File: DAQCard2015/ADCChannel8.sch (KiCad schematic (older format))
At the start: 21 parts, among them U10 THS4524IDBTR, U11 AD9219

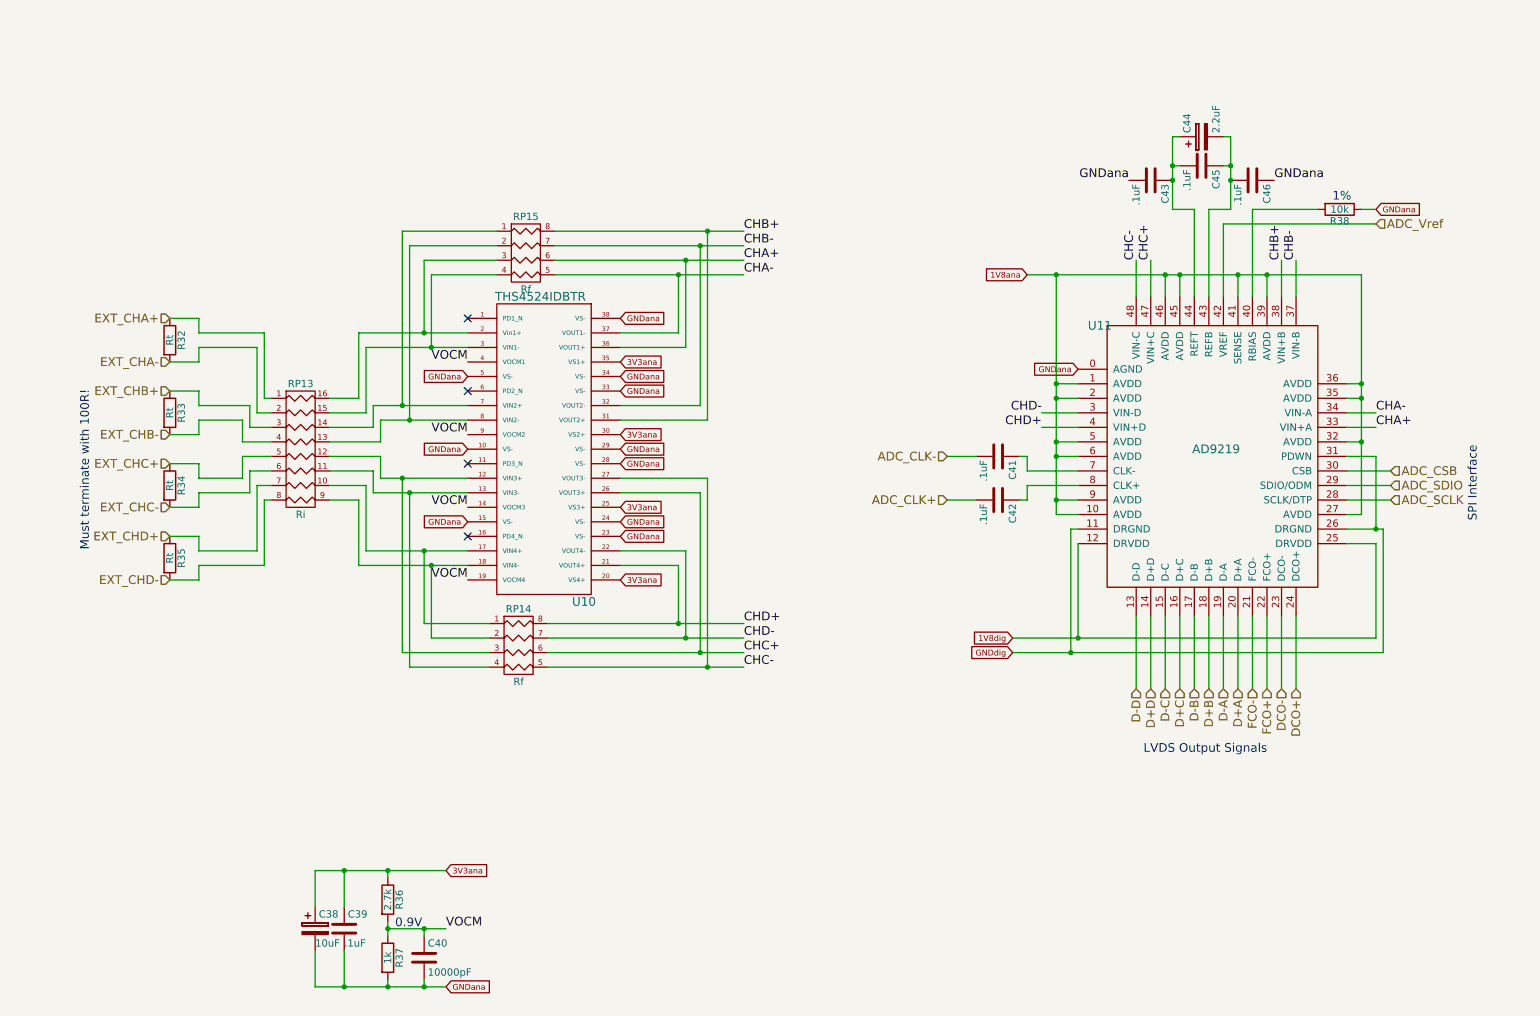
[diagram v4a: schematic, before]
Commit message: propogate previous changes to other channels and schematic
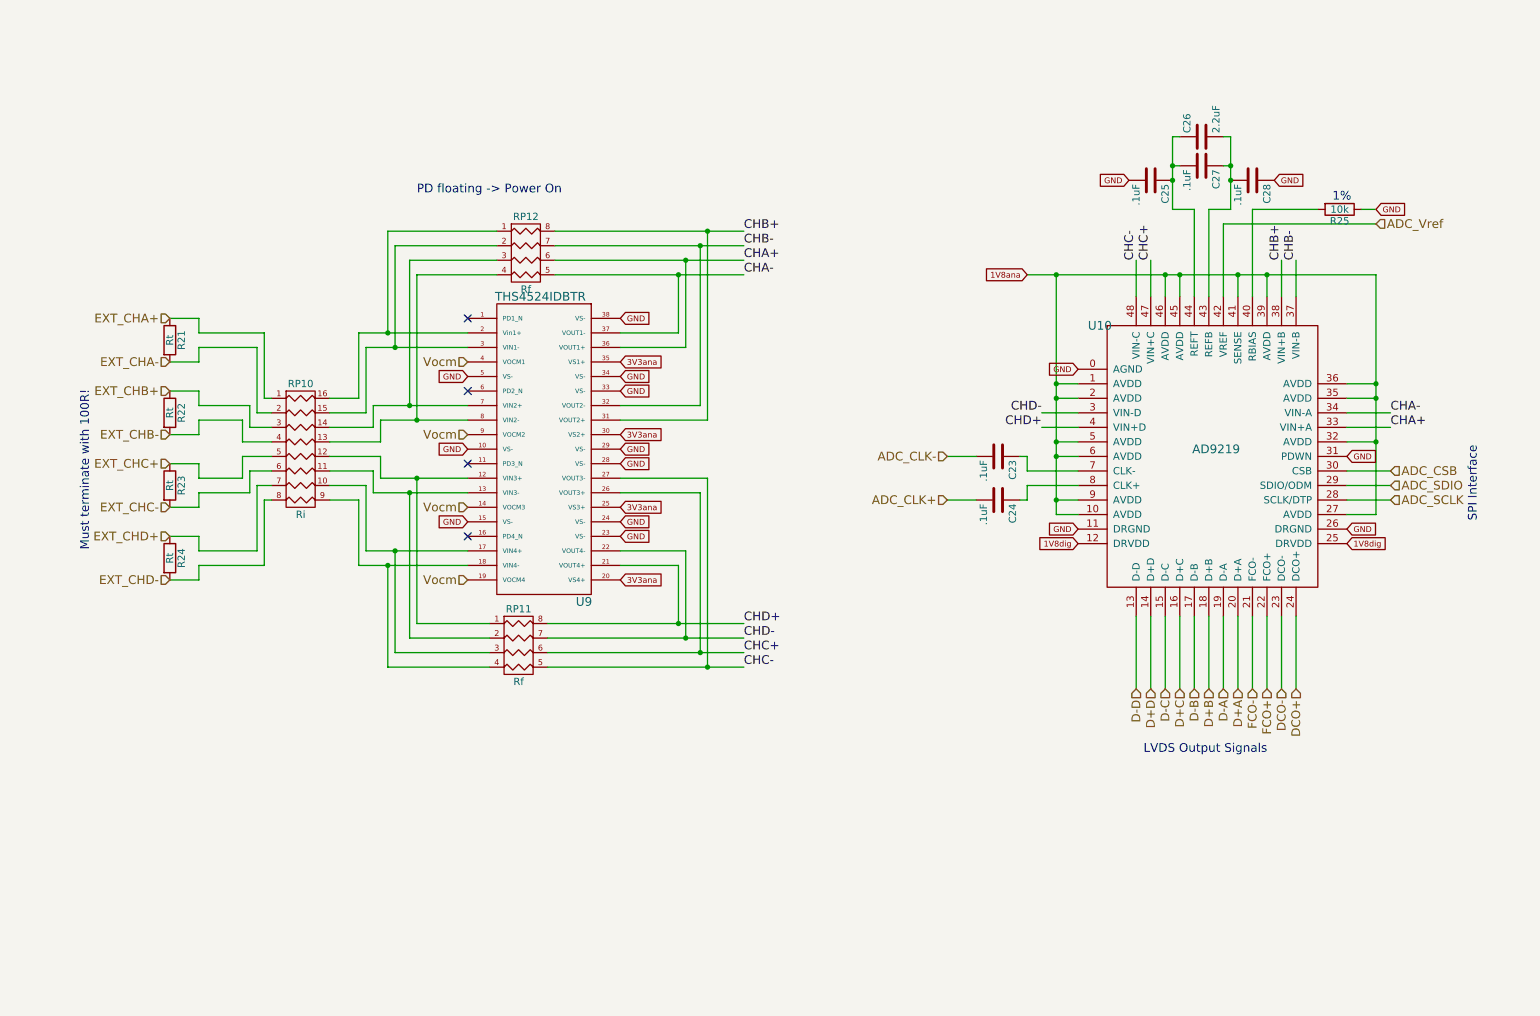
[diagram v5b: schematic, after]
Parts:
- removed C38: 10uF, Capacitors_SMD:C_0805, symbol CP
- removed C39, C41, C42, C43, C45, C46: .1uF, Capacitors_SMD:C_0603, symbol C
- removed C40: 10000pF, Capacitors_SMD:C_0603, symbol C
- removed C44: 2.2uF, Capacitors_SMD:C_0805, symbol CP
- removed R32, R33, R34, R35: Rt, Resistors_SMD:R_0603, symbol R
- removed R36: 2.7k, Resistors_SMD:R_0603, symbol R
- removed R37: 1k, Resistors_SMD:R_0603, symbol R
- removed R38: 10k, Resistors_SMD:R_0603, symbol R
- removed RP13: Ri, extras:R8_MNR18, symbol R_PACK8
- removed RP14, RP15: Rf, extras:R4-MNR04, symbol R_PACK4
- removed U10: THS4524IDBTR, Housings_SSOP:TSSOP-38_4.4x9.7mm_Pitch0.5mm, symbol THS4524IDBTR
- removed U11: AD9219, SMD_Packages:QFN-48-1EP, symbol AD9219
- added C23, C24, C25, C27, C28: .1uF, Capacitors_SMD:C_0603, symbol C
- added C26: 2.2uF, Capacitors_SMD:C_0805, symbol C
- added R21, R22, R23, R24: Rt, Resistors_SMD:R_0603, symbol R
- added R25: 10k, Resistors_SMD:R_0603, symbol R
- added RP10: Ri, extras:R8_MNR18, symbol R_PACK8
- added RP11, RP12: Rf, extras:R4-MNR04, symbol R_PACK4
- added U10: AD9219, extras:QFN-48-1EP, symbol AD9219
- added U9: THS4524IDBTR, Housings_SSOP:TSSOP-38_4.4x9.7mm_Pitch0.5mm, symbol THS4524IDBTR
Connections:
- net 1V8ana: now also U10.1 (AVDD), U10.10 (AVDD), U10.2 (AVDD), U10.27 (AVDD), U10.32 (AVDD), U10.35 (AVDD), U10.36 (AVDD), U10.39 (AVDD), U10.41 (SENSE), U10.45 (AVDD), U10.46 (AVDD), U10.5 (AVDD), U10.6 (AVDD), U10.9 (AVDD)
- net 1V8dig: now also U10.12 (DRVDD), U10.25 (DRVDD)
- net 3V3ana: now also U9.20 (VS4+), U9.25 (VS3+), U9.30 (VS2+), U9.35 (VS1+)
- net ADC_CLK+: now also C24.2
- net ADC_CLK-: now also C23.2
- net ADC_CSB: now also U10.30 (CSB)
- net ADC_SCLK: now also U10.28 (SCLK/DTP)
- net ADC_SDIO: now also U10.29 (SDIO/ODM)
- net ADC_Vref: now also U10.42 (VREF)
- net CHA+: now also RP12.6 (R3), U10.33 (VIN+A), U9.36 (VOUT1+)
- net CHA-: now also RP12.5 (R4), U10.34 (VIN-A), U9.37 (VOUT1-)
- net CHB+: now also RP12.8 (R1), U10.38 (VIN+B), U9.31 (VOUT2+)
- net CHB-: now also RP12.7 (R2), U10.37 (VIN-B), U9.32 (VOUT2-)
- net CHC+: now also RP11.6 (R3), U10.47 (VIN+C), U9.26 (VOUT3+)
- net CHC-: now also RP11.5 (R4), U10.48 (VIN-C), U9.27 (VOUT3-)
- net CHD+: now also RP11.8 (R1), U10.4 (VIN+D), U9.21 (VOUT4+)
- net CHD-: now also RP11.7 (R2), U10.3 (VIN-D), U9.22 (VOUT4-)
- net D+A: now also U10.20 (D+A)
- net D+B: now also U10.18 (D+B)
- net D+C: now also U10.16 (D+C)
- net D+D: now also U10.14 (D+D)
- net D-A: now also U10.19 (D-A)
- net D-B: now also U10.17 (D-B)
- net D-C: now also U10.15 (D-C)
- net D-D: now also U10.13 (D-D)
- net DCO+: now also U10.24 (DCO+)
- net DCO-: now also U10.23 (DCO-)
- net EXT_CHA+: now also R21.1, RP10.1 (P1)
- net EXT_CHA-: now also R21.2, RP10.2 (P2)
- net EXT_CHB+: now also R22.1, RP10.3 (P3)
- net EXT_CHB-: now also R22.2, RP10.4 (P4)
- net EXT_CHC+: now also R23.1, RP10.5 (P5)
- net EXT_CHC-: now also R23.2, RP10.6 (P6)
- net EXT_CHD+: now also R24.1, RP10.7 (P7)
- net EXT_CHD-: now also R24.2, RP10.8 (P8)
- net FCO+: now also U10.22 (FCO+)
- net FCO-: now also U10.21 (FCO-)
- new net: C24.1, U10.8 (CLK+)
- new net: RP10.16 (R1), RP12.1 (P1), U9.2 (Vin1+)
- new net: RP10.15 (R2), RP12.2 (P2), U9.3 (VIN1-)
- new net: RP10.14 (R3), RP12.3 (P3), U9.7 (VIN2+)
- new net: RP10.13 (R4), RP12.4 (P4), U9.8 (VIN2-)
- new net: R25.2, U10.40 (RBIAS)
- new net: C26.2, C27.1, C28.2, U10.43 (REFB)
- new net: C25.1, C26.1, C27.2, U10.44 (REFT)
- new net: C23.1, U10.7 (CLK-)
- new net: RP10.12 (R5), RP11.1 (P1), U9.12 (VIN3+)
- new net: RP10.11 (R6), RP11.2 (P2), U9.13 (VIN3-)
- new net: RP10.10 (R7), RP11.3 (P3), U9.17 (VIN4+)
- new net: RP10.9 (R8), RP11.4 (P4), U9.18 (VIN4-)
- new net GND: C25.2, C28.1, R25.1, U10.0 (AGND), U10.11 (DRGND), U10.26 (DRGND), U10.31 (PDWN), U9.10 (VS-), U9.15 (VS-), U9.23 (VS-), U9.24 (VS-), U9.28 (VS-), U9.29 (VS-), U9.33 (VS-), U9.34 (VS-), U9.38 (VS-), U9.5 (VS-)
- new net Vocm: U9.14 (VOCM3), U9.19 (VOCM4), U9.4 (VOCM1), U9.9 (VOCM2)
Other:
- note added: "PD floating -> Power On"
- note removed: "0.9V"

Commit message: Various updates to DAQ board focusing on power system
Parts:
- U9: footprint Housings_SSOP:TSSOP-38_4.4x9.7mm_Pitch0.5mm -> extras:TSSOP-38_4.4x9.7mm_Pitch0.5mm
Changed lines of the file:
@@
 F 0 "U9" H 4700 2750 60  0000 C CNN
 F 1 "THS4524IDBTR" H 4400 4850 60  0000 C CNN
-F 2 "Housings_SSOP:TSSOP-38_4.4x9.7mm_Pitch0.5mm" H 4600 3800 60  0001 C CNN
+F 2 "extras:TSSOP-38_4.4x9.7mm_Pitch0.5mm" H 4600 3800 60  0001 C CNN
 F 3 "" H 4600 3800 60  0000 C CNN
 	1    4400 3700

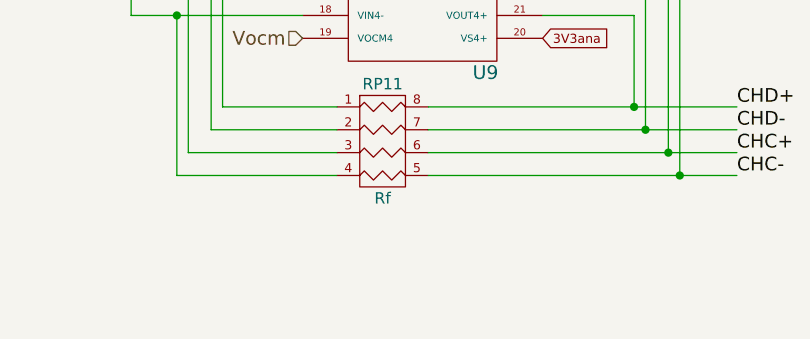
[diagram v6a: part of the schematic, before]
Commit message: Update to DAQ Board including adding an JTAG header and hooking up external clock and trigger
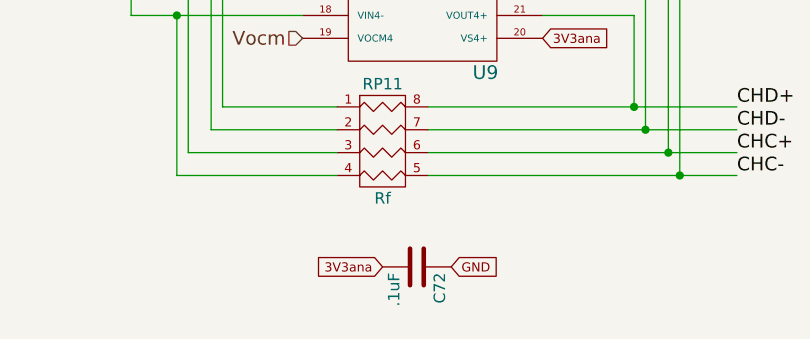
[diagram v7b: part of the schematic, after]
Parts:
- added C72: .1uF, Capacitors_SMD:C_0603, symbol C
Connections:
- net 3V3ana: now also C72.2
- net GND: now also C72.1
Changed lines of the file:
@@
 $Descr A4 11693 8268
 encoding utf-8
-Sheet 3 13
+Sheet 13 13
 Title ""
 Date ""
@@
 Text GLabel 8100 4150 0    40   Input ~ 0
 GND
+$Comp
+L C C72
+U 1 1 5605C69F
+P 4400 5500
+F 0 "C72" H 4425 5600 50  0000 L CNN
+F 1 ".1uF" H 4425 5400 50  0000 L CNN
+F 2 "Capacitors_SMD:C_0603" H 4438 5350 30  0001 C CNN
+F 3 "" H 4400 5500 60  0000 C CNN
+	1    4400 5500
+	0    1    1    0
+$EndComp
+Text GLabel 4250 5500 0    40   Input ~ 0
+3V3ana
+Text GLabel 4550 5500 2    40   Input ~ 0
+GND
 $EndSCHEMATC

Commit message: Adds digipart field to all parts that is now used in automatic generation of BOM(see DAQCard2015.html)
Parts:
- C23, C24, C25, C27, C28, C72: digipart (none) -> 445-1316-1-ND
- C26: digipart (none) -> 445-1420-1-ND
- R21, R22, R23, R24: digipart (none) -> P107HCT-ND
- R25: digipart (none) -> P10.0KHCT-ND
- RP10: digipart (none) -> RHM1564CT-ND
- RP11, RP12: digipart (none) -> RHM1336CT-ND
- U10: digipart (none) -> AD9219ABCPZ-40-ND
- U9: digipart (none) -> 296-24315-1-ND
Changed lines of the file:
@@
 F 2 "extras:QFN-48-1EP" H 8650 3700 60  0001 C CNN
 F 3 "" H 8650 3700 60  0000 C CNN
+F 4 "AD9219ABCPZ-40-ND" H 9050 3700 60  0001 C CNN "digipart"
 	1    9050 3700
 	1    0    0    -1
@@
 F 2 "Capacitors_SMD:C_0603" H 7588 3500 30  0001 C CNN
 F 3 "" H 7550 3650 60  0000 C CNN
+F 4 "445-1316-1-ND" H 7550 3650 60  0001 C CNN "digipart"
 	1    7550 3650
 	0    1    1    0
@@
 F 2 "Capacitors_SMD:C_0603" H 7588 3800 30  0001 C CNN
 F 3 "" H 7550 3950 60  0000 C CNN
+F 4 "445-1316-1-ND" H 7550 3950 60  0001 C CNN "digipart"
 	1    7550 3950
 	0    1    1    0
@@
 F 2 "Capacitors_SMD:C_0603" H 9338 1600 30  0001 C CNN
 F 3 "" H 9300 1750 60  0000 C CNN
+F 4 "445-1316-1-ND" H 9300 1750 60  0001 C CNN "digipart"
 	1    9300 1750
 	0    1    1    0
@@
 F 2 "Capacitors_SMD:C_0603" H 8638 1600 30  0001 C CNN
 F 3 "" H 8600 1750 60  0000 C CNN
+F 4 "445-1316-1-ND" H 8600 1750 60  0001 C CNN "digipart"
 	1    8600 1750
 	0    1    1    0
@@
 F 2 "Capacitors_SMD:C_0603" H 8988 1500 30  0001 C CNN
 F 3 "" H 8950 1650 60  0000 C CNN
+F 4 "445-1316-1-ND" H 8950 1650 60  0001 C CNN "digipart"
 	1    8950 1650
 	0    1    1    0
@@
 F 2 "Resistors_SMD:R_0603" V 9830 1950 30  0001 C CNN
 F 3 "" H 9900 1950 30  0000 C CNN
+F 4 "P10.0KHCT-ND" V 9900 1950 60  0001 C CNN "digipart"
 	1    9900 1950
 	0    1    1    0
@@
 F 2 "extras:TSSOP-38_4.4x9.7mm_Pitch0.5mm" H 4600 3800 60  0001 C CNN
 F 3 "" H 4600 3800 60  0000 C CNN
+F 4 "296-24315-1-ND" H 4400 3700 60  0001 C CNN "digipart"
 	1    4400 3700
 	1    0    0    -1
@@
 F 2 "Resistors_SMD:R_0603" V 1780 4350 30  0001 C CNN
 F 3 "" H 1850 4350 30  0000 C CNN
+F 4 "P107HCT-ND" V 1850 4350 60  0001 C CNN "digipart"
 	1    1850 4350
 	1    0    0    -1
@@
 F 2 "Resistors_SMD:R_0603" V 1780 3850 30  0001 C CNN
 F 3 "" H 1850 3850 30  0000 C CNN
+F 4 "P107HCT-ND" V 1850 3850 60  0001 C CNN "digipart"
 	1    1850 3850
 	1    0    0    -1
@@
 F 2 "Resistors_SMD:R_0603" V 1780 3350 30  0001 C CNN
 F 3 "" H 1850 3350 30  0000 C CNN
+F 4 "P107HCT-ND" V 1850 3350 60  0001 C CNN "digipart"
 	1    1850 3350
 	1    0    0    -1
@@
 F 2 "Resistors_SMD:R_0603" V 1780 2850 30  0001 C CNN
 F 3 "" H 1850 2850 30  0000 C CNN
+F 4 "P107HCT-ND" V 1850 2850 60  0001 C CNN "digipart"
 	1    1850 2850
 	1    0    0    -1
@@
 F 2 "extras:R4-MNR04" H 4250 5150 60  0001 C CNN
 F 3 "" H 4250 5150 60  0000 C CNN
+F 4 "RHM1336CT-ND" H 4250 5150 60  0001 C CNN "digipart"
 	1    4250 5150
 	1    0    0    -1
@@
 F 2 "extras:R4-MNR04" H 4300 2450 60  0001 C CNN
 F 3 "" H 4300 2450 60  0000 C CNN
+F 4 "RHM1336CT-ND" H 4300 2450 60  0001 C CNN "digipart"
 	1    4300 2450
 	1    0    0    -1
@@
 F 2 "extras:R8_MNR18" H 2750 3600 60  0001 C CNN
 F 3 "" H 2750 3600 60  0000 C CNN
+F 4 "RHM1564CT-ND" H 2750 3600 60  0001 C CNN "digipart"
 	1    2750 3600
 	1    0    0    -1
@@
 F 2 "Capacitors_SMD:C_0805" H 8988 1300 30  0001 C CNN
 F 3 "" H 8950 1450 60  0000 C CNN
+F 4 "445-1420-1-ND" H 8950 1450 60  0001 C CNN "digipart"
 	1    8950 1450
 	0    -1   -1   0
@@
 F 2 "Capacitors_SMD:C_0603" H 4438 5350 30  0001 C CNN
 F 3 "" H 4400 5500 60  0000 C CNN
+F 4 "445-1316-1-ND" H 4400 5500 60  0001 C CNN "digipart"
 	1    4400 5500
 	0    1    1    0
